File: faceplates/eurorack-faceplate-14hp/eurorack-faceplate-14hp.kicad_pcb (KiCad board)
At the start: 2 copper layers, 70.8 x 133.3 mm, 4 parts

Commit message: Moving mounting holes
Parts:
- moved REF** 2.42 mm to (5.08, 130.3)
- moved REF** 2.42 mm to (5.08, 3.00)
- moved REF** 2.34 mm to (65.7, 130.3)
- moved REF** 2.34 mm to (65.7, 3.00)
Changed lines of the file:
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@@
   (net 0 "")
   (footprint "MountingHole:MountingHole_3.2mm_M3" (layer "F.Cu")
-    (at 7.5 130.35)
+    (at 5.08 130.35)
     (descr "Mounting Hole 3.2mm, no annular, M3")
     (tags "mounting hole 3.2mm no annular m3")
@@
   )
   (footprint "MountingHole:MountingHole_3.2mm_M3" (layer "F.Cu")
-    (at 63.38 130.35)
+    (at 65.72 130.35)
     (descr "Mounting Hole 3.2mm, no annular, M3")
     (tags "mounting hole 3.2mm no annular m3")
@@
   )
   (footprint "MountingHole:MountingHole_3.2mm_M3" (layer "F.Cu")
-    (at 63.38 3)
+    (at 65.72 3)
     (descr "Mounting Hole 3.2mm, no annular, M3")
     (tags "mounting hole 3.2mm no annular m3")
@@
   )
   (footprint "MountingHole:MountingHole_3.2mm_M3" (layer "F.Cu")
-    (at 7.5 3)
+    (at 5.08 3)
     (descr "Mounting Hole 3.2mm, no annular, M3")
     (tags "mounting hole 3.2mm no annular m3")

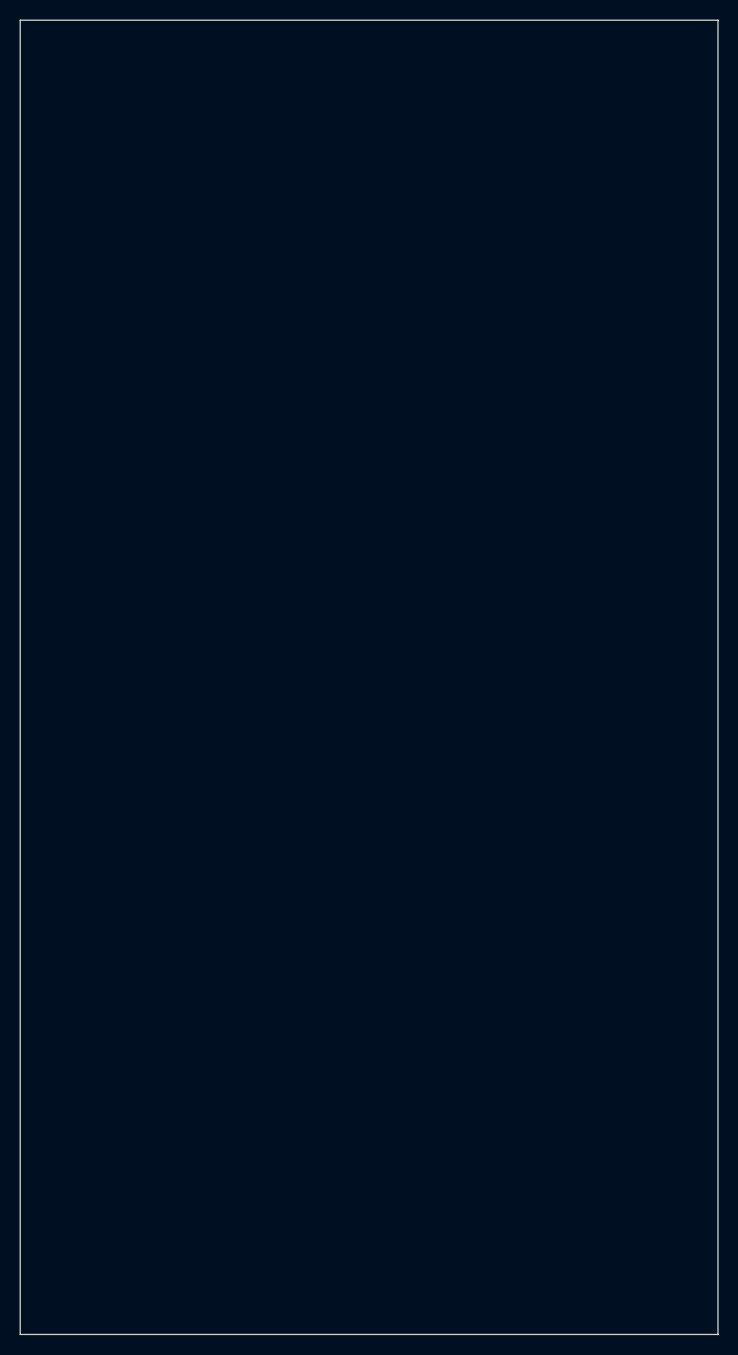
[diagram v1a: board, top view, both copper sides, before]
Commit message: Correcting panel height
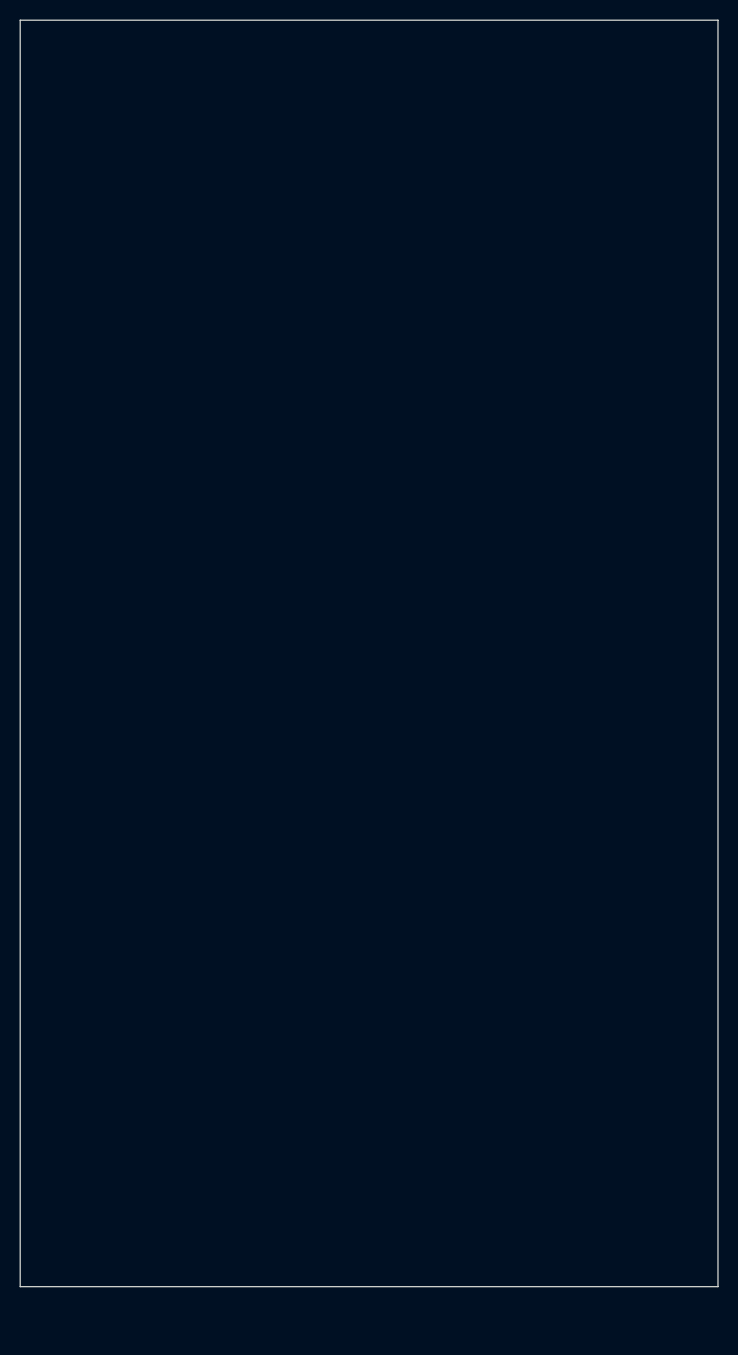
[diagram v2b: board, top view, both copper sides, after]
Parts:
- moved REF** 4.85 mm to (5.08, 125.5)
- moved REF** 4.85 mm to (65.7, 125.5)
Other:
- board size 70.8 x 133.3 mm -> 70.8 x 128.5 mm
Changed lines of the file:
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@@
   (net 0 "")
   (footprint "MountingHole:MountingHole_3.2mm_M3" (layer "F.Cu")
-    (at 5.08 130.35)
+    (at 5.08 125.5)
     (descr "Mounting Hole 3.2mm, no annular, M3")
     (tags "mounting hole 3.2mm no annular m3")
@@
   )
   (footprint "MountingHole:MountingHole_3.2mm_M3" (layer "F.Cu")
-    (at 65.72 130.35)
+    (at 65.72 125.5)
     (descr "Mounting Hole 3.2mm, no annular, M3")
     (tags "mounting hole 3.2mm no annular m3")
@@
     (pad "" np_thru_hole oval locked (at 0 0) (size 7 3.2) (drill oval 7 3.2) (layers F&B.Cu *.Mask))
   )
-  (gr_line (start 70.8 0) (end 70.8 133.35) (layer "Edge.Cuts") (width 0.1))
-  (gr_line (start 0 133.35) (end 0 0) (layer "Edge.Cuts") (width 0.1))
+  (gr_line (start 70.8 0) (end 70.8 128.5) (layer "Edge.Cuts") (width 0.1))
+  (gr_line (start 0 128.5) (end 0 0) (layer "Edge.Cuts") (width 0.1))
   (gr_line (start 0 0) (end 70.8 0) (layer "Edge.Cuts") (width 0.1))
-  (gr_line (start 70.8 133.35) (end 0 133.35) (layer "Edge.Cuts") (width 0.1))
+  (gr_line (start 70.8 128.5) (end 0 128.5) (layer "Edge.Cuts") (width 0.1))
 )
